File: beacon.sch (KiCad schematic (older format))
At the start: 45 parts, among them U1 NUF2042VX6, U2 SN65HVD256, U3 MPU-9250, U4 LT1965-3.3, U5 STM32F405RGT6, U6 DWM1000, X1 16MHz

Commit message: Update with first corrections from review
Add reset button
Fix CAN wiring
Add test pads on SPI buses
Fix MCU pin name
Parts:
- added SW1: RST, symbol SW_PUSH_SMALL
- added W1: TEST_UWB_CSN, symbol TEST
- added W2: TEST_UWB_CLK, symbol TEST
- added W3: TEST_UWB_MISO, symbol TEST
- added W4: TEST_UWB_MOSi, symbol TEST
- added W5: TEST_IMU_CSN, symbol TEST
- added W6: TEST_IMU_CLK, symbol TEST
- added W7: TEST_IMU_MISO, symbol TEST
- added W8: TEST_IMU_MOSi, symbol TEST
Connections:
- wire segments 286 -> 237
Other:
- moved on the sheet: C10, C11, C12, C13, C14, C15, C16, C6, C7, D10, D3, D4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

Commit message: Update with further corrections from review
LED resistors 330 so we sink ~3mA at 3.3V
Fix NUF2042XV6 name
Fix MPU9205 wiring (contradictory datasheet)
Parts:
- removed U1: NUF2042VX6, symbol NUF2042VX6
- added U1: NUF2042XV6, symbol NUF2042XV6
- RP1, RP2: value 1k -> 330
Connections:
- wire segments 237 -> 297
- no-connect marks 46 -> 45

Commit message: Place components, first try
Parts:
- removed RP1, RP2: 330, symbol R_PACK4
- added R10, R3, R4, R5, R6, R7, R8, R9: 330, Resistors_SMD:R_0603, symbol R_Small
- C1, C11, C12, C13, C15, C16, C17, C18, C2, C3, C4, C5, C6, C7, C8, C9: footprint (none) -> Capacitors_SMD:C_0603
- C10: footprint (none) -> Capacitors_SMD:C_1206
- C14: footprint (none) -> Capacitors_SMD:C_0805
- CONN1: footprint (none) -> _connectors:_Micro-USB-AB-receptacle-SMT-th
- CONN2, CONN3: footprint MODULE -> _connectors:_Molex-PicoBlade-SMD-4
- CONN4: footprint MODULE -> _connectors:_Molex-PicoBlade-SMD-7
- D1, D2: footprint (none) -> _std:_SOD-323
- D10, D3, D4, D5, D6, D7, D8, D9: footprint (none) -> _std:_LED_0603
- F1, F2: footprint (none) -> Resistors_SMD:R_1206
- R1, R2: footprint (none) -> Resistors_SMD:R_0603
- SW1: footprint (none) -> _div:_PTS525SK15-SMT-Pushbutton
- U1: footprint (none) -> _std:SOT-563_6-lead
- U2: footprint MODULE -> _std:_SO-8
- U3: footprint (none) -> _sensors:_MPU-9XX0
- U4: footprint MODULE -> Housings_DFN_QFN:DFN-8-1EP_3x3mm_Pitch0.5mm
- U5: footprint MODULE -> _lqfp:_LQFP64
- U6: footprint (none) -> _div:DWM1000
- W1, W2, W3, W4, W5, W6, W7, W8: footprint (none) -> _std:Measurement_Point_Round-SMD-Pad_Small
- X1: footprint (none) -> _div:XTAL_ABMM2
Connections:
- wire segments 297 -> 221

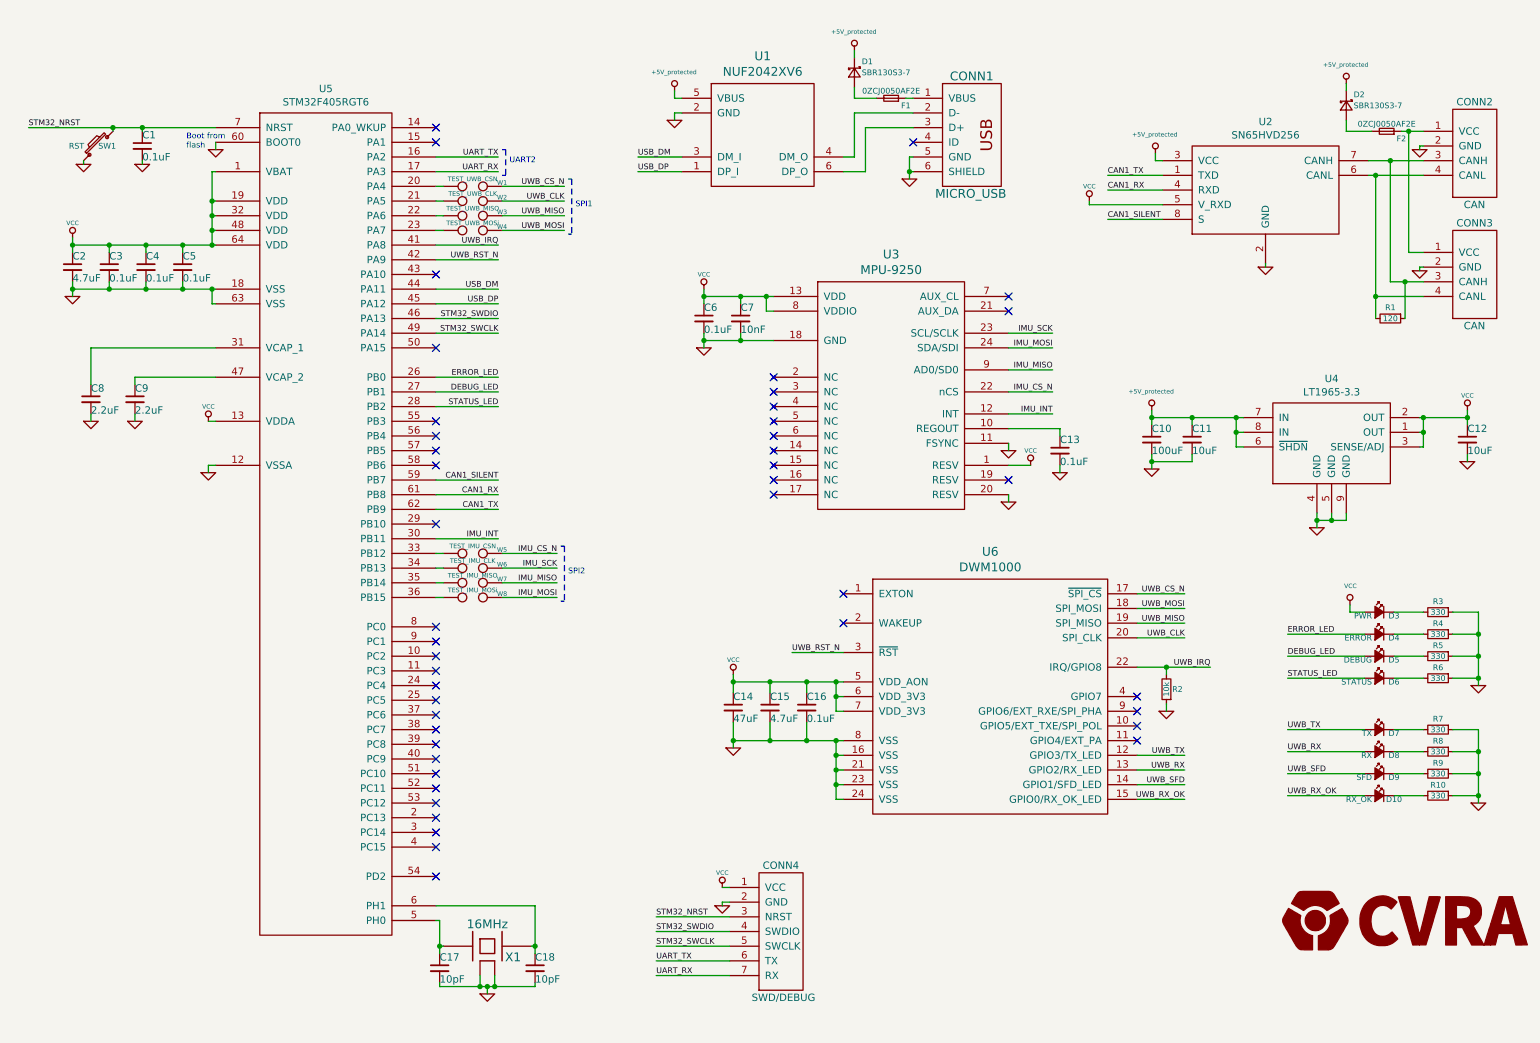
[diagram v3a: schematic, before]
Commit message: Add mounting holes and fix testpads
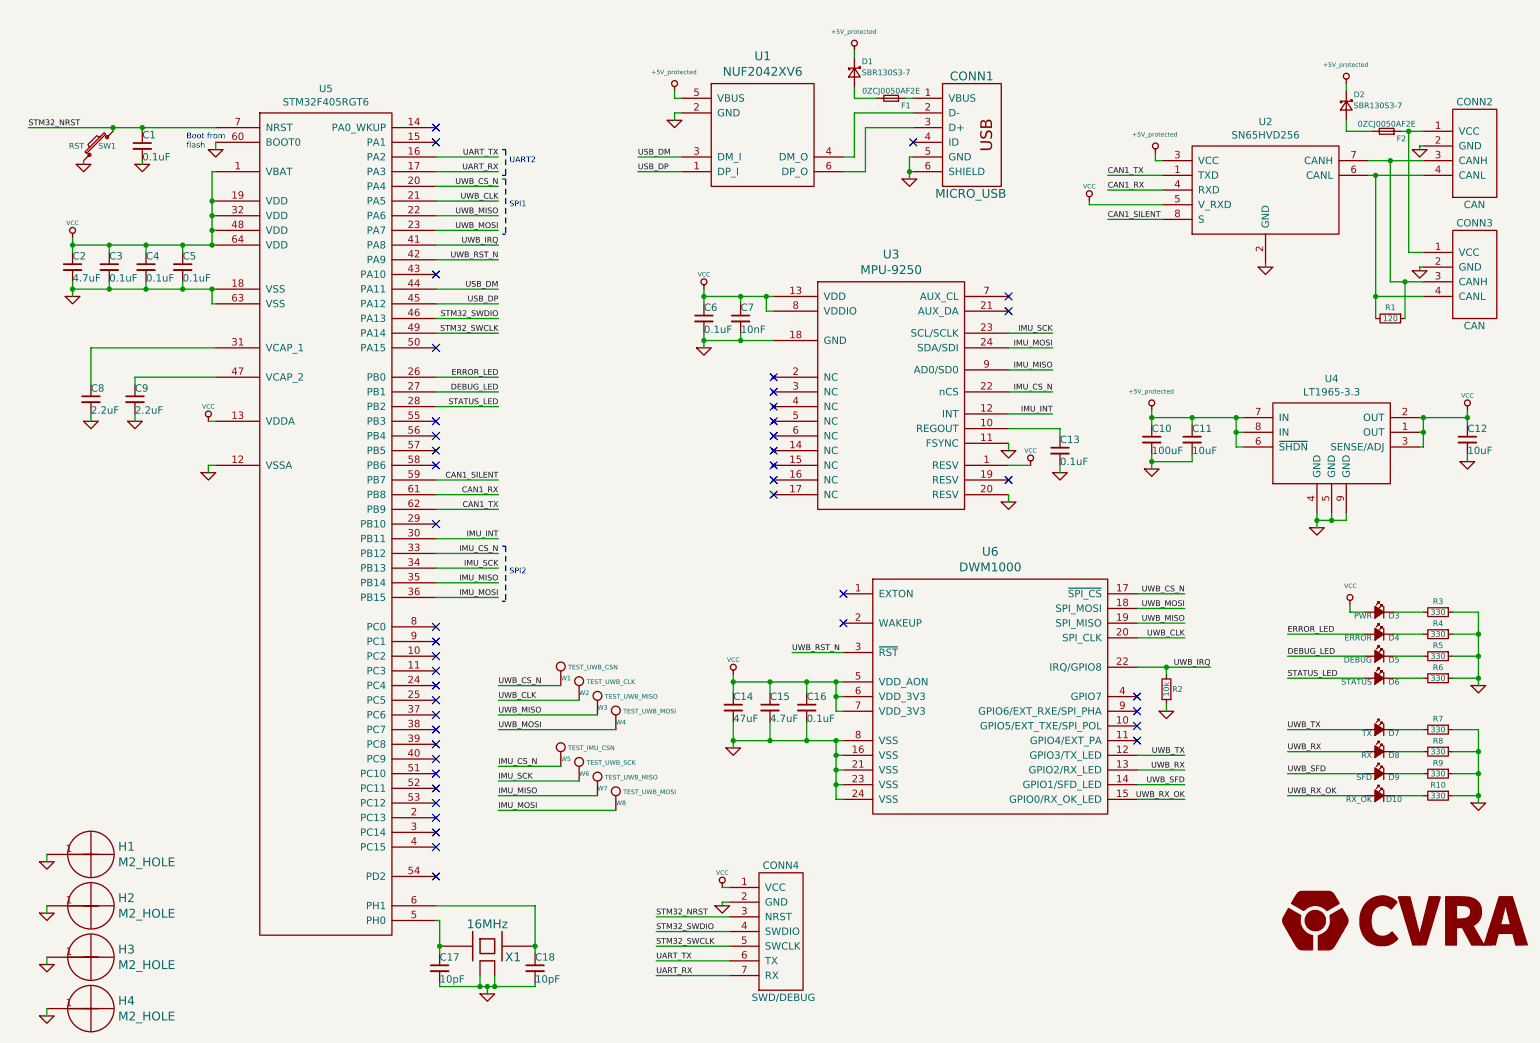
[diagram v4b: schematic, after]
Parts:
- removed W1: TEST_UWB_CSN, _std:Measurement_Point_Round-SMD-Pad_Small, symbol TEST
- removed W2: TEST_UWB_CLK, _std:Measurement_Point_Round-SMD-Pad_Small, symbol TEST
- removed W3: TEST_UWB_MISO, _std:Measurement_Point_Round-SMD-Pad_Small, symbol TEST
- removed W4: TEST_UWB_MOSi, _std:Measurement_Point_Round-SMD-Pad_Small, symbol TEST
- removed W5: TEST_IMU_CSN, _std:Measurement_Point_Round-SMD-Pad_Small, symbol TEST
- removed W6: TEST_IMU_CLK, _std:Measurement_Point_Round-SMD-Pad_Small, symbol TEST
- removed W7: TEST_IMU_MISO, _std:Measurement_Point_Round-SMD-Pad_Small, symbol TEST
- removed W8: TEST_IMU_MOSi, _std:Measurement_Point_Round-SMD-Pad_Small, symbol TEST
- added H1, H2, H3, H4: M2_HOLE, _mech:_M2, symbol HOLE
- added W1: TEST_UWB_CSN, _div:Test_1pin_SMD, symbol TEST_1P
- added W2: TEST_UWB_CLK, _div:Test_1pin_SMD, symbol TEST_1P
- added W3, W7: TEST_UWB_MISO, _div:Test_1pin_SMD, symbol TEST_1P
- added W4, W8: TEST_UWB_MOSI, _div:Test_1pin_SMD, symbol TEST_1P
- added W5: TEST_IMU_CSN, _div:Test_1pin_SMD, symbol TEST_1P
- added W6: TEST_UWB_SCK, _div:Test_1pin_SMD, symbol TEST_1P
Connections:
- net GND: now also H1.1, H2.1, H3.1, H4.1
- net IMU_CS_N: now also U5.33 (PB12), W5.1
- net IMU_MISO: now also U5.35 (PB14), W7.1
- net IMU_MOSI: now also U5.36 (PB15), W8.1
- net IMU_SCK: now also U5.34 (PB13), W6.1
- net UWB_CLK: now also U5.21 (PA5), W2.1
- net UWB_CS_N: now also U5.20 (PA4), W1.1
- net UWB_MISO: now also U5.22 (PA6), W3.1
- net UWB_MOSI: now also U5.23 (PA7), W4.1

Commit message: Corrections from review remarks
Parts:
- C1, C11, C12, C13, C15, C16, C17, C18, C2, C3, C4, C5, C6, C7, C8, C9: footprint Capacitors_SMD:C_0603 -> _std:C_0603
- C10: footprint Capacitors_SMD:C_1206 -> _std:C_1206
- C14: footprint Capacitors_SMD:C_0805 -> _std:C_0805
- D10, D3, D4, D5, D6, D7, D8, D9: footprint _std:_LED_0603 -> _std:D_0603
- F1, F2: footprint Resistors_SMD:R_1206 -> _std:R_1206
- R1, R10, R2, R3, R4, R5, R6, R7, R8, R9: footprint Resistors_SMD:R_0603 -> _std:R_0603
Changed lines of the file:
@@
 F 0 "C1" H 1525 1625 50  0000 L CNN
 F 1 "0.1uF" H 1525 1475 50  0000 L CNN
-F 2 "Capacitors_SMD:C_0603" H 1525 1550 50  0001 C CNN
+F 2 "_std:C_0603" H 1525 1550 50  0001 C CNN
 F 3 "" H 1525 1550 50  0000 C CNN
 	1    1525 1550
@@
 F 0 "C5" H 1800 2450 50  0000 L CNN
 F 1 "0.1uF" H 1800 2300 50  0000 L CNN
-F 2 "Capacitors_SMD:C_0603" H 1800 2375 50  0001 C CNN
+F 2 "_std:C_0603" H 1800 2375 50  0001 C CNN
 F 3 "" H 1800 2375 50  0000 C CNN
 	1    1800 2375
@@
 F 0 "C4" H 1550 2450 50  0000 L CNN
 F 1 "0.1uF" H 1550 2300 50  0000 L CNN
-F 2 "Capacitors_SMD:C_0603" H 1550 2375 50  0001 C CNN
+F 2 "_std:C_0603" H 1550 2375 50  0001 C CNN
 F 3 "" H 1550 2375 50  0000 C CNN
 	1    1550 2375
@@
 F 0 "C3" H 1300 2450 50  0000 L CNN
 F 1 "0.1uF" H 1300 2300 50  0000 L CNN
-F 2 "Capacitors_SMD:C_0603" H 1300 2375 50  0001 C CNN
+F 2 "_std:C_0603" H 1300 2375 50  0001 C CNN
 F 3 "" H 1300 2375 50  0000 C CNN
 	1    1300 2375
@@
 F 0 "C17" H 3550 7225 50  0000 L CNN
 F 1 "10pF" H 3550 7075 50  0000 L CNN
-F 2 "Capacitors_SMD:C_0603" H 3550 7150 50  0001 C CNN
+F 2 "_std:C_0603" H 3550 7150 50  0001 C CNN
 F 3 "" H 3550 7150 50  0000 C CNN
 	1    3550 7150
@@
 F 0 "C18" H 4200 7225 50  0000 L CNN
 F 1 "10pF" H 4200 7075 50  0000 L CNN
-F 2 "Capacitors_SMD:C_0603" H 4200 7150 50  0001 C CNN
+F 2 "_std:C_0603" H 4200 7150 50  0001 C CNN
 F 3 "" H 4200 7150 50  0000 C CNN
 	1    4200 7150
@@
 F 0 "C2" H 1050 2450 50  0000 L CNN
 F 1 "4.7uF" H 1050 2300 50  0000 L CNN
-F 2 "Capacitors_SMD:C_0603" H 1050 2375 50  0001 C CNN
+F 2 "_std:C_0603" H 1050 2375 50  0001 C CNN
 F 3 "" H 1050 2375 50  0000 C CNN
 	1    1050 2375
@@
 F 0 "C16" H 6050 5450 50  0000 L CNN
 F 1 "0.1uF" H 6050 5300 50  0000 L CNN
-F 2 "Capacitors_SMD:C_0603" H 6050 5375 50  0001 C CNN
+F 2 "_std:C_0603" H 6050 5375 50  0001 C CNN
 F 3 "" H 6050 5375 50  0000 C CNN
 	1    6050 5375
@@
 F 0 "C15" H 5800 5450 50  0000 L CNN
 F 1 "4.7uF" H 5800 5300 50  0000 L CNN
-F 2 "Capacitors_SMD:C_0603" H 5800 5375 50  0001 C CNN
+F 2 "_std:C_0603" H 5800 5375 50  0001 C CNN
 F 3 "" H 5800 5375 50  0000 C CNN
 	1    5800 5375
@@
 F 0 "C14" H 5550 5450 50  0000 L CNN
 F 1 "47uF" H 5550 5300 50  0000 L CNN
-F 2 "Capacitors_SMD:C_0805" H 5550 5375 50  0001 C CNN
+F 2 "_std:C_0805" H 5550 5375 50  0001 C CNN
 F 3 "" H 5550 5375 50  0000 C CNN
 	1    5550 5375
@@
 F 0 "R2" H 8425 5250 39  0000 C CNN
 F 1 "10k" V 8500 5250 39  0000 C CNN
-F 2 "Resistors_SMD:R_0603" H 8500 5250 50  0001 C CNN
+F 2 "_std:R_0603" H 8500 5250 50  0001 C CNN
 F 3 "" H 8500 5250 50  0000 C CNN
 	1    8500 5250
@@
 F 0 "D7" H 9850 5500 39  0000 C CNN
 F 1 "TX" H 10000 5500 39  0000 L CNN
-F 2 "_std:_LED_0603" V 9950 5525 50  0001 C CNN
+F 2 "_std:D_0603" V 9950 5525 50  0001 C CNN
 F 3 "" V 9950 5525 50  0000 C CNN
 	1    9950 5525
@@
 F 0 "D8" H 9850 5650 39  0000 C CNN
 F 1 "RX" H 10000 5650 39  0000 L CNN
-F 2 "_std:_LED_0603" V 9950 5675 50  0001 C CNN
+F 2 "_std:D_0603" V 9950 5675 50  0001 C CNN
 F 3 "" V 9950 5675 50  0000 C CNN
 	1    9950 5675
@@
 F 0 "D9" H 9850 5800 39  0000 C CNN
 F 1 "SFD" H 10000 5800 39  0000 L CNN
-F 2 "_std:_LED_0603" V 9950 5825 50  0001 C CNN
+F 2 "_std:D_0603" V 9950 5825 50  0001 C CNN
 F 3 "" V 9950 5825 50  0000 C CNN
 	1    9950 5825
@@
 F 0 "D10" H 9850 5950 39  0000 C CNN
 F 1 "RX_OK" H 10000 5950 39  0000 L CNN
-F 2 "_std:_LED_0603" V 9950 5975 50  0001 C CNN
+F 2 "_std:D_0603" V 9950 5975 50  0001 C CNN
 F 3 "" V 9950 5975 50  0000 C CNN
 	1    9950 5975
@@
 F 0 "F1" H 6525 1275 39  0000 C CNN
 F 1 "0ZCJ0050AF2E" H 6625 1175 39  0000 C CNN
-F 2 "Resistors_SMD:R_1206" H 6625 1225 50  0001 C CNN
+F 2 "_std:R_1206" H 6625 1225 50  0001 C CNN
 F 3 "" H 6625 1225 50  0000 C CNN
 	1    6625 1225
@@
 F 0 "C7" H 5600 2800 50  0000 L CNN
 F 1 "10nF" H 5600 2650 50  0000 L CNN
-F 2 "Capacitors_SMD:C_0603" H 5600 2725 50  0001 C CNN
+F 2 "_std:C_0603" H 5600 2725 50  0001 C CNN
 F 3 "" H 5600 2725 50  0000 C CNN
 	1    5600 2725
@@
 F 0 "C6" H 5350 2800 50  0000 L CNN
 F 1 "0.1uF" H 5350 2650 50  0000 L CNN
-F 2 "Capacitors_SMD:C_0603" H 5350 2725 50  0001 C CNN
+F 2 "_std:C_0603" H 5350 2725 50  0001 C CNN
 F 3 "" H 5350 2725 50  0000 C CNN
 	1    5350 2725
@@
 F 0 "C13" H 7775 3700 50  0000 L CNN
 F 1 "0.1uF" H 7775 3550 50  0000 L CNN
-F 2 "Capacitors_SMD:C_0603" H 7775 3625 50  0001 C CNN
+F 2 "_std:C_0603" H 7775 3625 50  0001 C CNN
 F 3 "" H 7775 3625 50  0000 C CNN
 	1    7775 3625
@@
 F 0 "R1" V 9950 2725 39  0000 C CNN
 F 1 "120" V 10025 2725 39  0000 C CNN
-F 2 "Resistors_SMD:R_0603" H 10025 2725 50  0001 C CNN
+F 2 "_std:R_0603" H 10025 2725 50  0001 C CNN
 F 3 "" H 10025 2725 50  0000 C CNN
 	1    10025 2725
@@
 F 0 "F2" H 9900 1500 39  0000 C CNN
 F 1 "0ZCJ0050AF2E" H 10000 1400 39  0000 C CNN
-F 2 "Resistors_SMD:R_1206" H 10000 1450 50  0001 C CNN
+F 2 "_std:R_1206" H 10000 1450 50  0001 C CNN
 F 3 "" H 10000 1450 50  0000 C CNN
 	1    10000 1450
@@
 F 0 "C11" H 8675 3625 50  0000 L CNN
 F 1 "10uF" H 8675 3475 50  0000 L CNN
-F 2 "Capacitors_SMD:C_0603" H 8675 3550 50  0001 C CNN
+F 2 "_std:C_0603" H 8675 3550 50  0001 C CNN
 F 3 "" H 8675 3550 50  0000 C CNN
 	1    8675 3550
@@
 F 0 "C10" H 8400 3625 50  0000 L CNN
 F 1 "100uF" H 8400 3475 50  0000 L CNN
-F 2 "Capacitors_SMD:C_1206" H 8400 3550 50  0001 C CNN
+F 2 "_std:C_1206" H 8400 3550 50  0001 C CNN
 F 3 "" H 8400 3550 50  0000 C CNN
 	1    8400 3550
@@
 F 0 "C12" H 10550 3625 50  0000 L CNN
 F 1 "10uF" H 10550 3475 50  0000 L CNN
-F 2 "Capacitors_SMD:C_0603" H 10550 3550 50  0001 C CNN
+F 2 "_std:C_0603" H 10550 3550 50  0001 C CNN
 F 3 "" H 10550 3550 50  0000 C CNN
 	1    10550 3550
@@
 F 0 "D3" H 9850 4700 39  0000 C CNN
 F 1 "PWR" H 10000 4700 39  0000 L CNN
-F 2 "_std:_LED_0603" V 9950 4725 50  0001 C CNN
+F 2 "_std:D_0603" V 9950 4725 50  0001 C CNN
 F 3 "" V 9950 4725 50  0000 C CNN
 	1    9950 4725
@@
 F 0 "D4" H 9850 4850 39  0000 C CNN
 F 1 "ERROR" H 10000 4850 39  0000 L CNN
-F 2 "_std:_LED_0603" V 9950 4875 50  0001 C CNN
+F 2 "_std:D_0603" V 9950 4875 50  0001 C CNN
 F 3 "" V 9950 4875 50  0000 C CNN
 	1    9950 4875
@@
 F 0 "D5" H 9850 5000 39  0000 C CNN
 F 1 "DEBUG" H 10000 5000 39  0000 L CNN
-F 2 "_std:_LED_0603" V 9950 5025 50  0001 C CNN
+F 2 "_std:D_0603" V 9950 5025 50  0001 C CNN
 F 3 "" V 9950 5025 50  0000 C CNN
 	1    9950 5025
@@
 F 0 "D6" H 9850 5150 39  0000 C CNN
 F 1 "STATUS" H 10000 5150 39  0000 L CNN
-F 2 "_std:_LED_0603" V 9950 5175 50  0001 C CNN
+F 2 "_std:D_0603" V 9950 5175 50  0001 C CNN
 F 3 "" V 9950 5175 50  0000 C CNN
 	1    9950 5175
@@
 F 0 "C9" H 1475 3350 50  0000 L CNN
 F 1 "2.2uF" H 1475 3200 50  0000 L CNN
-F 2 "Capacitors_SMD:C_0603" H 1475 3275 50  0001 C CNN
+F 2 "_std:C_0603" H 1475 3275 50  0001 C CNN
 F 3 "" H 1475 3275 50  0000 C CNN
 	1    1475 3275
@@
 F 0 "C8" H 1175 3350 50  0000 L CNN
 F 1 "2.2uF" H 1175 3200 50  0000 L CNN
-F 2 "Capacitors_SMD:C_0603" H 1175 3275 50  0001 C CNN
+F 2 "_std:C_0603" H 1175 3275 50  0001 C CNN
 F 3 "" H 1175 3275 50  0000 C CNN
 	1    1175 3275
@@
 F 0 "R3" V 10300 4725 39  0000 C BNN
 F 1 "330" V 10350 4725 39  0000 C CNN
-F 2 "Resistors_SMD:R_0603" H 10350 4725 50  0001 C CNN
+F 2 "_std:R_0603" H 10350 4725 50  0001 C CNN
 F 3 "" H 10350 4725 50  0000 C CNN
 	1    10350 4725
@@
 F 0 "R4" V 10300 4875 39  0000 C BNN
 F 1 "330" V 10350 4875 39  0000 C CNN
-F 2 "Resistors_SMD:R_0603" H 10350 4875 50  0001 C CNN
+F 2 "_std:R_0603" H 10350 4875 50  0001 C CNN
 F 3 "" H 10350 4875 50  0000 C CNN
 	1    10350 4875
@@
 F 0 "R5" V 10300 5025 39  0000 C BNN
 F 1 "330" V 10350 5025 39  0000 C CNN
-F 2 "Resistors_SMD:R_0603" H 10350 5025 50  0001 C CNN
+F 2 "_std:R_0603" H 10350 5025 50  0001 C CNN
 F 3 "" H 10350 5025 50  0000 C CNN
 	1    10350 5025
@@
 F 0 "R6" V 10300 5175 39  0000 C BNN
 F 1 "330" V 10350 5175 39  0000 C CNN
-F 2 "Resistors_SMD:R_0603" H 10350 5175 50  0001 C CNN
+F 2 "_std:R_0603" H 10350 5175 50  0001 C CNN
 F 3 "" H 10350 5175 50  0000 C CNN
 	1    10350 5175
@@
 F 0 "R7" V 10300 5525 39  0000 C BNN
 F 1 "330" V 10350 5525 39  0000 C CNN
-F 2 "Resistors_SMD:R_0603" H 10350 5525 50  0001 C CNN
+F 2 "_std:R_0603" H 10350 5525 50  0001 C CNN
 F 3 "" H 10350 5525 50  0000 C CNN
 	1    10350 5525
@@
 F 0 "R8" V 10300 5675 39  0000 C BNN
 F 1 "330" V 10350 5675 39  0000 C CNN
-F 2 "Resistors_SMD:R_0603" H 10350 5675 50  0001 C CNN
+F 2 "_std:R_0603" H 10350 5675 50  0001 C CNN
 F 3 "" H 10350 5675 50  0000 C CNN
 	1    10350 5675
@@
 F 0 "R9" V 10300 5825 39  0000 C BNN
 F 1 "330" V 10350 5825 39  0000 C CNN
-F 2 "Resistors_SMD:R_0603" H 10350 5825 50  0001 C CNN
+F 2 "_std:R_0603" H 10350 5825 50  0001 C CNN
 F 3 "" H 10350 5825 50  0000 C CNN
 	1    10350 5825
@@
 F 0 "R10" V 10300 5975 39  0000 C BNN
 F 1 "330" V 10350 5975 39  0000 C CNN
-F 2 "Resistors_SMD:R_0603" H 10350 5975 50  0001 C CNN
+F 2 "_std:R_0603" H 10350 5975 50  0001 C CNN
 F 3 "" H 10350 5975 50  0000 C CNN
 	1    10350 5975

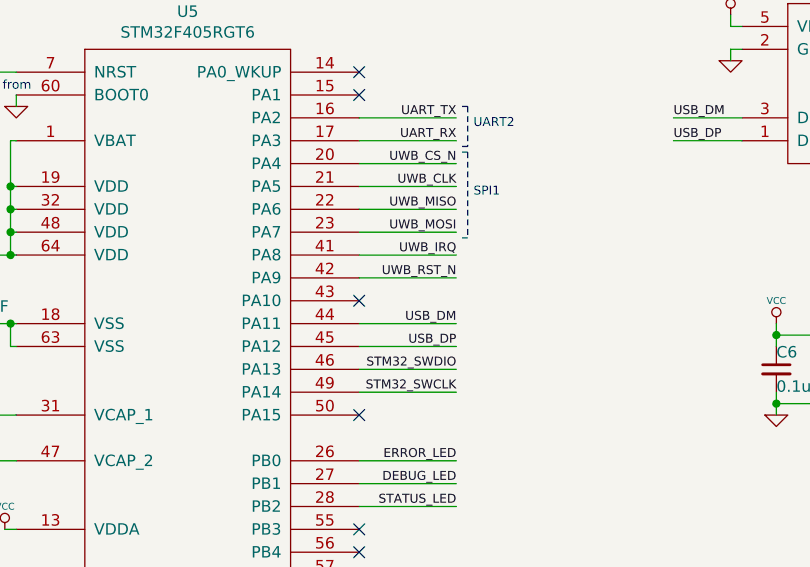
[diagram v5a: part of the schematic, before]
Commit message: Rewire UWB reset to not interfere with VUSB sense
Fixes #2
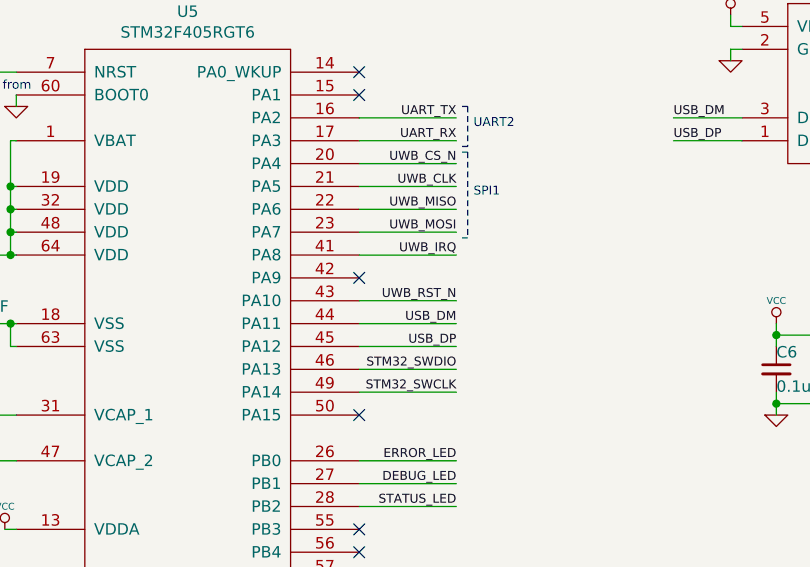
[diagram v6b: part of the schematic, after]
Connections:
- net UWB_RST_N: now also U5.43 (PA10); no longer U5.42 (PA9)
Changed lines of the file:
@@
 Text Label 3950 1925 2    39   ~ 0
 UWB_CLK
-Text Label 3950 2325 2    39   ~ 0
+Text Label 3950 2425 2    39   ~ 0
 UWB_RST_N
 Text Label 3950 2225 2    39   ~ 0
@@
 NoConn ~ 3525 1425
 NoConn ~ 3525 1525
-NoConn ~ 3525 2425
+NoConn ~ 3525 2325
 NoConn ~ 3525 2925
 NoConn ~ 3525 3425
@@
 	3950 1925 3525 1925
 Wire Wire Line
-	3950 2325 3525 2325
+	3950 2425 3525 2425
 Wire Wire Line
 	3950 2225 3525 2225
